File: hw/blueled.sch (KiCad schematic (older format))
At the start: 56 parts, among them J1 Barrel_Jack, J2 LED Strip, J3 ICSP, J4 Screw_Terminal_01x02, Q1 Q_PMOS_SDG, Q2 Q_PNP_EBC, SW2 PUSH, U1 ATmega328P-AU, U2 HC-05, U3 AMS1117-3.3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

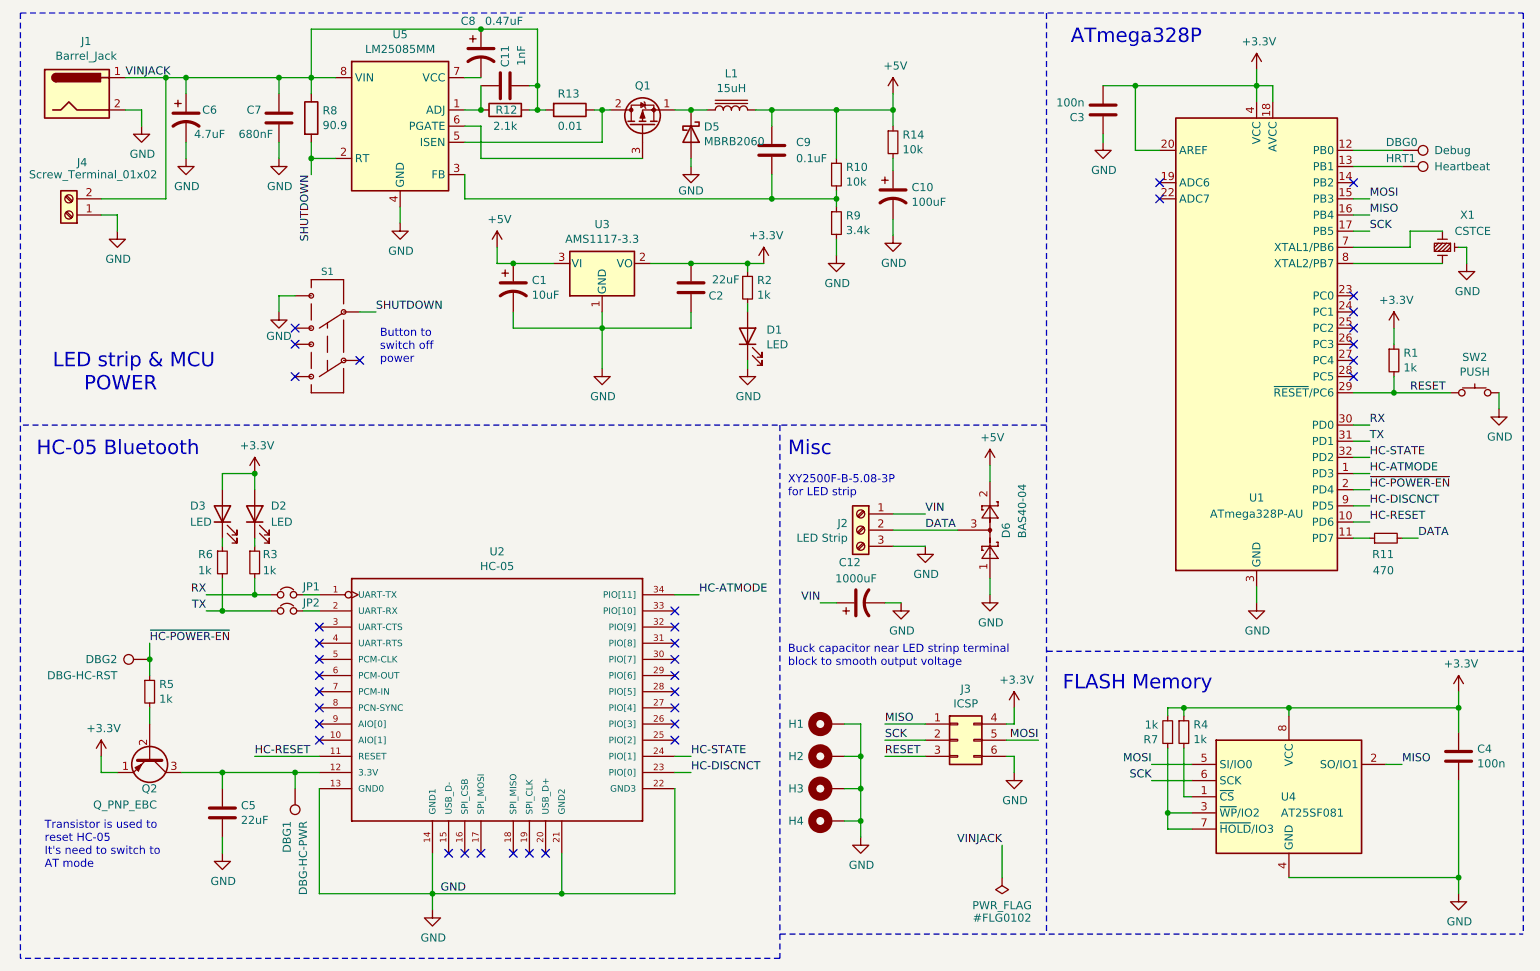
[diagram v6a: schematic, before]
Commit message: add(hw): component assignment is done
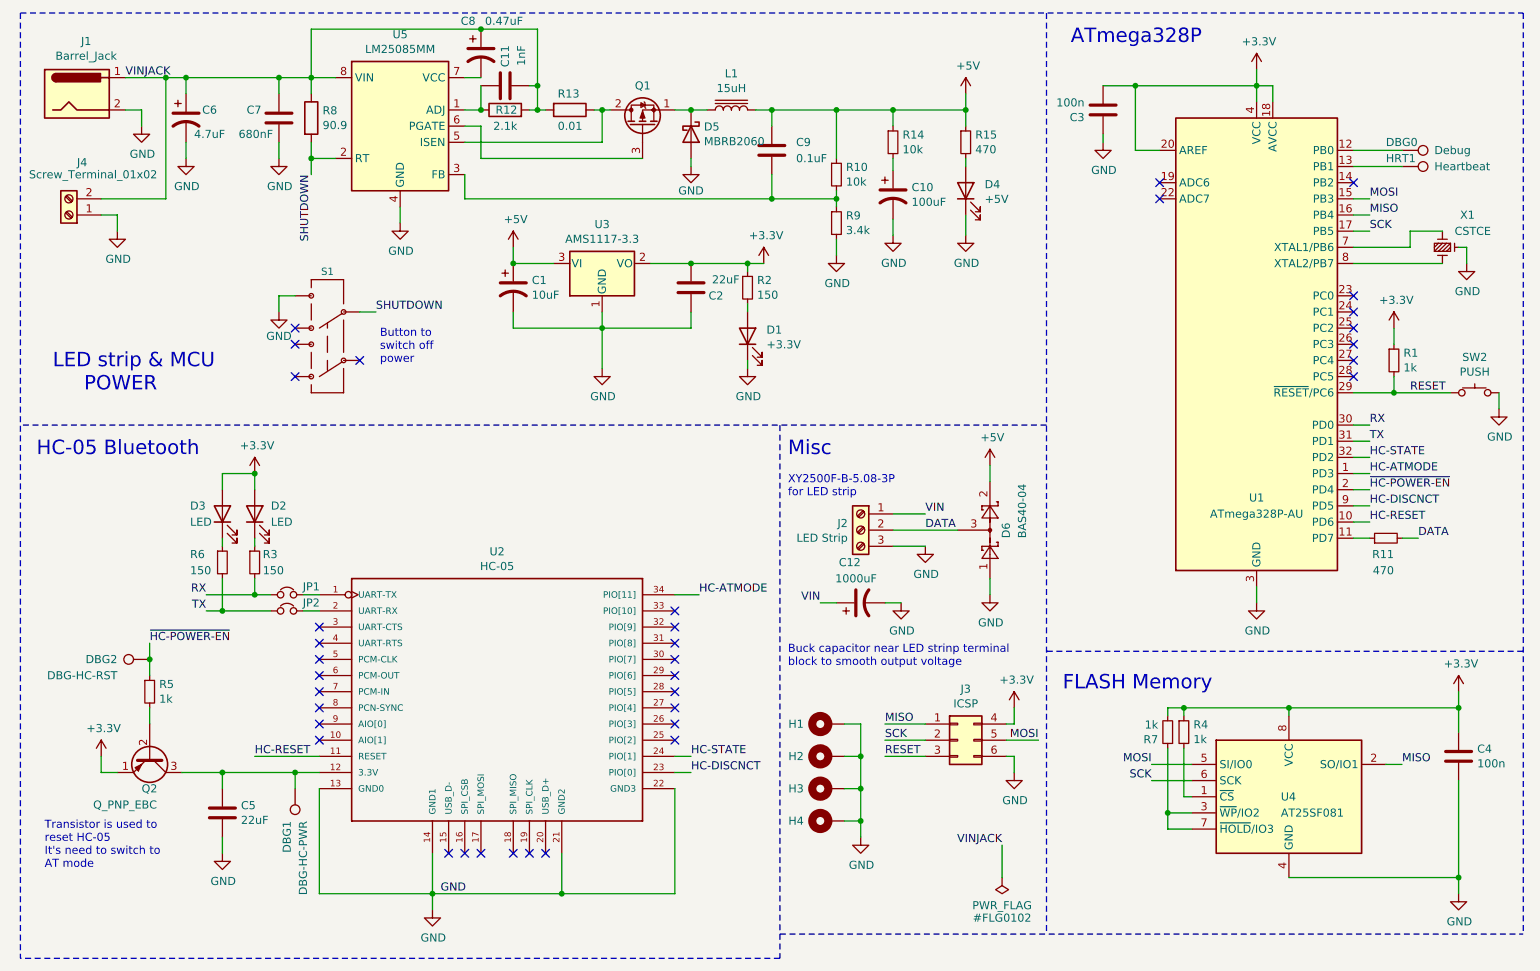
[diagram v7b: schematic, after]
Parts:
- added D4: +5V, LED_SMD:LED_0805_2012Metric_Pad1.15x1.40mm_HandSolder, symbol Device:LED
- added R15: 470, Resistor_SMD:R_0805_2012Metric_Pad1.15x1.40mm_HandSolder, symbol Device:R_Small
- D1: value LED -> +3.3V
- R2, R3, R6: value 1k -> 150; Manuf. Part RC0805FR-071KL -> RC0805FR-07150RL
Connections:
- net +5V: now also R15.1
- net GND: now also D4.1 (K)
- new net: D4.2 (A), R15.2
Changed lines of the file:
@@
 Wire Wire Line
 	3650 2450 3650 2550
-Wire Wire Line
-	3650 2550 4200 2550
 Connection ~ 4200 2550
 $Comp
@@
 P 5100 2300
 F 0 "R2" H 5159 2346 50  0000 L CNN
-F 1 "1k" H 5159 2255 50  0000 L CNN
+F 1 "150" H 5159 2255 50  0000 L CNN
 F 2 "Resistor_SMD:R_0805_2012Metric_Pad1.15x1.40mm_HandSolder" H 5100 2300 50  0001 C CNN
-F 3 "https://datasheet.lcsc.com/szlcsc/1810010118_YAGEO-RC0805FR-071KL_C95781.pdf" H 5100 2300 50  0001 C CNN
+F 3 "https://datasheet.lcsc.com/szlcsc/YAGEO-RC0805FR-07150RL_C114523.pdf" H 5100 2300 50  0001 C CNN
 F 4 "lcsc.com" H 5100 2300 50  0001 C CNN "Distributor"
-F 5 "RC0805FR-071KL" H 5100 2300 50  0001 C CNN "Manuf. Part"
+F 5 "RC0805FR-07150RL" H 5100 2300 50  0001 C CNN "Manuf. Part"
 	1    5100 2300
 	1    0    0    -1
@@
 P 5100 2600
 F 0 "D1" V 5139 2483 50  0000 R CNN
-F 1 "LED" V 5048 2483 50  0000 R CNN
+F 1 "+3.3V" V 5048 2483 50  0000 R CNN
 F 2 "LED_SMD:LED_0805_2012Metric_Pad1.15x1.40mm_HandSolder" H 5100 2600 50  0001 C CNN
 F 3 "https://datasheet.lcsc.com/szlcsc/1811141223_TOGIALED-TJ-S1608SW6TGLC2G-A5_C192316.pdf" H 5100 2600 50  0001 C CNN
@@
 U 1 1 5ED22AEB
 P 1850 4000
-F 0 "R6" H 1700 4050 50  0000 L CNN
-F 1 "1k" H 1700 3950 50  0000 L CNN
+F 0 "R6" H 1650 4050 50  0000 L CNN
+F 1 "150" H 1650 3950 50  0000 L CNN
 F 2 "Resistor_SMD:R_0805_2012Metric_Pad1.15x1.40mm_HandSolder" H 1850 4000 50  0001 C CNN
-F 3 "https://datasheet.lcsc.com/szlcsc/1810010118_YAGEO-RC0805FR-071KL_C95781.pdf" H 1850 4000 50  0001 C CNN
+F 3 "https://datasheet.lcsc.com/szlcsc/YAGEO-RC0805FR-07150RL_C114523.pdf" H 1850 4000 50  0001 C CNN
 F 4 "lcsc.com" H 1850 4000 50  0001 C CNN "Distributor"
-F 5 "RC0805FR-071KL" H 1850 4000 50  0001 C CNN "Manuf. Part"
+F 5 "RC0805FR-07150RL" H 1850 4000 50  0001 C CNN "Manuf. Part"
 	1    1850 4000
 	1    0    0    -1
@@
 P 2050 4000
 F 0 "R3" H 2100 4050 50  0000 L CNN
-F 1 "1k" H 2100 3950 50  0000 L CNN
+F 1 "150" H 2100 3950 50  0000 L CNN
 F 2 "Resistor_SMD:R_0805_2012Metric_Pad1.15x1.40mm_HandSolder" H 2050 4000 50  0001 C CNN
-F 3 "https://datasheet.lcsc.com/szlcsc/1810010118_YAGEO-RC0805FR-071KL_C95781.pdf" H 2050 4000 50  0001 C CNN
+F 3 "https://datasheet.lcsc.com/szlcsc/YAGEO-RC0805FR-07150RL_C114523.pdf" H 2050 4000 50  0001 C CNN
 F 4 "lcsc.com" H 2050 4000 50  0001 C CNN "Distributor"
-F 5 "RC0805FR-071KL" H 2050 4000 50  0001 C CNN "Manuf. Part"
+F 5 "RC0805FR-07150RL" H 2050 4000 50  0001 C CNN "Manuf. Part"
 	1    2050 4000
 	1    0    0    -1
@@
 Wire Wire Line
 	2300 5300 2450 5300
-$Comp
-L Device:CP1 C1
-U 1 1 5EA4B8BA
-P 3650 2300
-F 0 "C1" H 3765 2346 50  0000 L CNN
-F 1 "10uF" H 3765 2255 50  0000 L CNN
-F 2 "Capacitor_Tantalum_SMD:CP_EIA-3216-18_Kemet-A_Pad1.58x1.35mm_HandSolder" H 3650 2300 50  0001 C CNN
-F 3 "https://datasheet.lcsc.com/szlcsc/AVX-TAJA106K016RNJ_C7171.pdf" H 3650 2300 50  0001 C CNN
-F 4 "lcsc.com" H 3650 2300 50  0001 C CNN "Distributor"
-F 5 "TAJA106K016RNJ" H 3650 2300 50  0001 C CNN "Manuf. Part"
-	1    3650 2300
-	1    0    0    -1
-$EndComp
-Wire Wire Line
-	3550 2150 3650 2150
-Connection ~ 3650 2150
-Wire Wire Line
-	3650 2150 3900 2150
 Connection ~ 4750 2150
 Wire Wire Line
@@
 Wire Wire Line
 	4750 2550 4750 2450
-Wire Wire Line
-	4200 2550 4750 2550
 $Comp
 L Device:Jumper_NC_Small JP1
@@
 L power:+5V #PWR020
 U 1 1 5FF5B0B2
-P 6000 1100
-F 0 "#PWR020" H 6000 950 50  0001 C CNN
-F 1 "+5V" H 6015 1273 50  0000 C CNN
-F 2 "" H 6000 1100 50  0001 C CNN
-F 3 "" H 6000 1100 50  0001 C CNN
-	1    6000 1100
+P 6450 1100
+F 0 "#PWR020" H 6450 950 50  0001 C CNN
+F 1 "+5V" H 6465 1273 50  0000 C CNN
+F 2 "" H 6450 1100 50  0001 C CNN
+F 3 "" H 6450 1100 50  0001 C CNN
+	1    6450 1100
 	1    0    0    -1
 $EndComp
@@
 L power:+5V #PWR016
 U 1 1 5FF84E86
-P 3550 2050
-F 0 "#PWR016" H 3550 1900 50  0001 C CNN
-F 1 "+5V" H 3565 2223 50  0000 C CNN
-F 2 "" H 3550 2050 50  0001 C CNN
-F 3 "" H 3550 2050 50  0001 C CNN
-	1    3550 2050
-	1    0    0    -1
-$EndComp
-Wire Wire Line
-	3550 2150 3550 2050
+P 3650 2050
+F 0 "#PWR016" H 3650 1900 50  0001 C CNN
+F 1 "+5V" H 3665 2223 50  0000 C CNN
+F 2 "" H 3650 2050 50  0001 C CNN
+F 3 "" H 3650 2050 50  0001 C CNN
+	1    3650 2050
+	1    0    0    -1
+$EndComp
+Wire Wire Line
+	3650 2150 3650 2050
 $Comp
 L Diode:BAS40-04 D6
@@
 $EndComp
 Wire Wire Line
-	6000 1100 6000 1200
+	6450 1100 6450 1200
 Wire Wire Line
 	5250 1200 5650 1200
@@
 	5650 1200 6000 1200
 Connection ~ 5650 1200
-Connection ~ 6000 1200
 Wire Wire Line
 	6000 1200 6000 1300
@@
 	-1   0    0    1
 $EndComp
+$Comp
+L Device:R_Small R15
+U 1 1 5FF22C54
+P 6450 1400
+F 0 "R15" H 6509 1446 50  0000 L CNN
+F 1 "470" H 6509 1355 50  0000 L CNN
+F 2 "Resistor_SMD:R_0805_2012Metric_Pad1.15x1.40mm_HandSolder" H 6450 1400 50  0001 C CNN
+F 3 "https://datasheet.lcsc.com/szlcsc/1810311431_YAGEO-RC0805FR-07470RL_C114564.pdf" H 6450 1400 50  0001 C CNN
+F 4 "lcsc.com" H 6450 1400 50  0001 C CNN "Distributor"
+F 5 "RC0805FR-07470RL" H 6450 1400 50  0001 C CNN "Manuf. Part"
+	1    6450 1400
+	1    0    0    -1
+$EndComp
+$Comp
+L Device:LED D4
+U 1 1 5FF22C5C
+P 6450 1700
+F 0 "D4" V 6489 1583 50  0000 R CNN
+F 1 "+5V" V 6398 1583 50  0000 R CNN
+F 2 "LED_SMD:LED_0805_2012Metric_Pad1.15x1.40mm_HandSolder" H 6450 1700 50  0001 C CNN
+F 3 "https://datasheet.lcsc.com/szlcsc/1811141223_TOGIALED-TJ-S1608SW6TGLC2G-A5_C192316.pdf" H 6450 1700 50  0001 C CNN
+F 4 "lcsc.com" H 6450 1700 50  0001 C CNN "Distributor"
+F 5 "TJ-S1608SW6TGLC2G-A5 " H 6450 1700 50  0001 C CNN "Manuf. Part"
+	1    6450 1700
+	0    -1   -1   0
+$EndComp
+Wire Wire Line
+	6450 1500 6450 1550
+$Comp
+L power:GND #PWR024
+U 1 1 5FF22C63
+P 6450 1975
+F 0 "#PWR024" H 6450 1725 50  0001 C CNN
+F 1 "GND" H 6455 1802 50  0000 C CNN
+F 2 "" H 6450 1975 50  0001 C CNN
+F 3 "" H 6450 1975 50  0001 C CNN
+	1    6450 1975
+	1    0    0    -1
+$EndComp
+Wire Wire Line
+	6000 1200 6450 1200
+Connection ~ 6000 1200
+Wire Wire Line
+	6450 1300 6450 1200
+Connection ~ 6450 1200
+Wire Wire Line
+	6450 1850 6450 1975
+Wire Wire Line
+	3650 2550 4200 2550
+$Comp
+L Device:CP1 C1
+U 1 1 5EA4B8BA
+P 3650 2300
+F 0 "C1" H 3765 2346 50  0000 L CNN
+F 1 "10uF" H 3765 2255 50  0000 L CNN
+F 2 "Capacitor_Tantalum_SMD:CP_EIA-3216-18_Kemet-A_Pad1.58x1.35mm_HandSolder" H 3650 2300 50  0001 C CNN
+F 3 "https://datasheet.lcsc.com/szlcsc/AVX-TAJA106K016RNJ_C7171.pdf" H 3650 2300 50  0001 C CNN
+F 4 "lcsc.com" H 3650 2300 50  0001 C CNN "Distributor"
+F 5 "TAJA106K016RNJ" H 3650 2300 50  0001 C CNN "Manuf. Part"
+	1    3650 2300
+	1    0    0    -1
+$EndComp
+Wire Wire Line
+	4200 2550 4750 2550
+Wire Wire Line
+	3650 2150 3900 2150
+Connection ~ 3650 2150
 $EndSCHEMATC

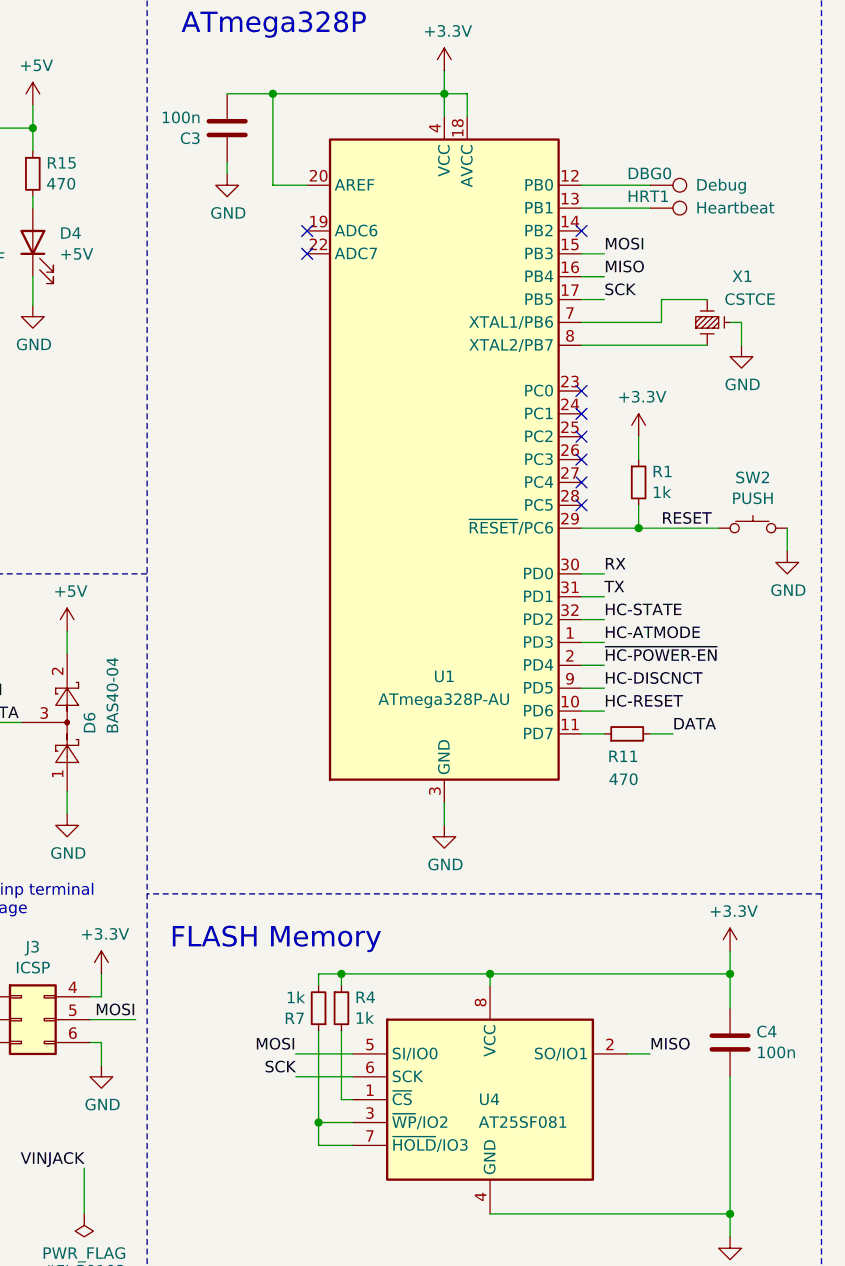
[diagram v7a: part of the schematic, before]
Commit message: add(hw): CS-FLASH connection
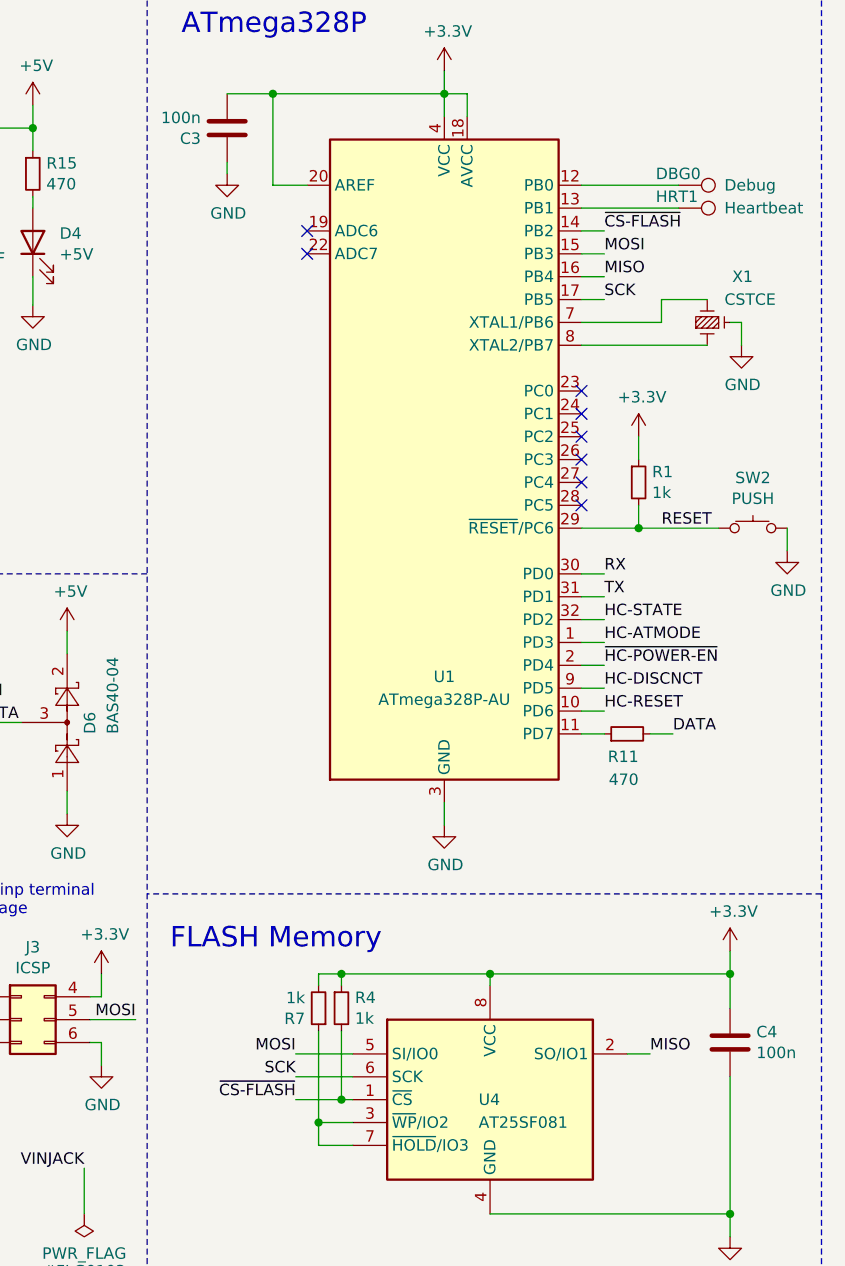
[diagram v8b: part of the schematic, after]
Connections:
- net ~CS-FLASH: now reaches U1.14 (PB2)
- net ~CS-FLASH: now also R4.2, U4.1 (~CS)
- no-connect marks 36 -> 35
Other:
- moved on the sheet: DBG0, HRT1
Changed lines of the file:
@@
 L Connector:TestPoint DBG0
 U 1 1 5D573650
-P 9150 1450
-F 0 "DBG0" V 9100 1350 50  0000 L CNN
-F 1 "Debug" V 9150 1650 50  0000 L CNN
-F 2 "TestPoint:TestPoint_Pad_D1.0mm" H 9350 1450 50  0001 C CNN
-F 3 "~" H 9350 1450 50  0001 C CNN
-	1    9150 1450
+P 9275 1450
+F 0 "DBG0" V 9225 1350 50  0000 L CNN
+F 1 "Debug" V 9275 1650 50  0000 L CNN
+F 2 "TestPoint:TestPoint_Pad_D1.0mm" H 9475 1450 50  0001 C CNN
+F 3 "~" H 9475 1450 50  0001 C CNN
+	1    9275 1450
 	0    1    1    0
 $EndComp
-Wire Wire Line
-	8850 1450 9150 1450
 $Comp
 L Memory_Flash:AT25SF081-SSHF-X U4
@@
 	9100 2950 9450 2950
 Connection ~ 9100 2950
-NoConn ~ 8850 1650
 $Comp
 L blueled-rescue:MOUDLE-BLUETOOTH-HC-05(34P-27X13MM)-MOUDLE-BLUETOOTH-HC-05_34P-27X13MM_ U2
@@
 L Connector:TestPoint HRT1
 U 1 1 5FA7C739
-P 9150 1550
-F 0 "HRT1" V 9100 1450 50  0000 L CNN
-F 1 "Heartbeat" V 9150 1750 50  0000 L CNN
-F 2 "TestPoint:TestPoint_Pad_D1.0mm" H 9350 1550 50  0001 C CNN
-F 3 "~" H 9350 1550 50  0001 C CNN
-	1    9150 1550
+P 9275 1550
+F 0 "HRT1" V 9225 1450 50  0000 L CNN
+F 1 "Heartbeat" V 9275 1750 50  0000 L CNN
+F 2 "TestPoint:TestPoint_Pad_D1.0mm" H 9475 1550 50  0001 C CNN
+F 3 "~" H 9475 1550 50  0001 C CNN
+	1    9275 1550
 	0    1    1    0
 $EndComp
-Wire Wire Line
-	8850 1550 9150 1550
 NoConn ~ 7650 1650
 Wire Wire Line
@@
 	3650 2150 3900 2150
 Connection ~ 3650 2150
+Text Label 8950 1650 0    50   ~ 0
+~CS-FLASH
+Wire Wire Line
+	8850 1650 8950 1650
+Wire Wire Line
+	8850 1450 9275 1450
+Wire Wire Line
+	8850 1550 9275 1550
+Text Label 7600 5450 2    50   ~ 0
+~CS-FLASH
+Wire Wire Line
+	7600 5450 7800 5450
+Connection ~ 7800 5450
 $EndSCHEMATC
